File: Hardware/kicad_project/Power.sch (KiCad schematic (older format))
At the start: 23 parts, among them J7 battery, J8 Conn_01x03_Male, Q1 DMG2305UX-13, Q2 Q_PMOS_GSD, Q3 Q_NPN_BEC, SW1 spst_4_pin_internal, U6 MCP73831T-2ATI_OT, U7 AMS1117-3.3

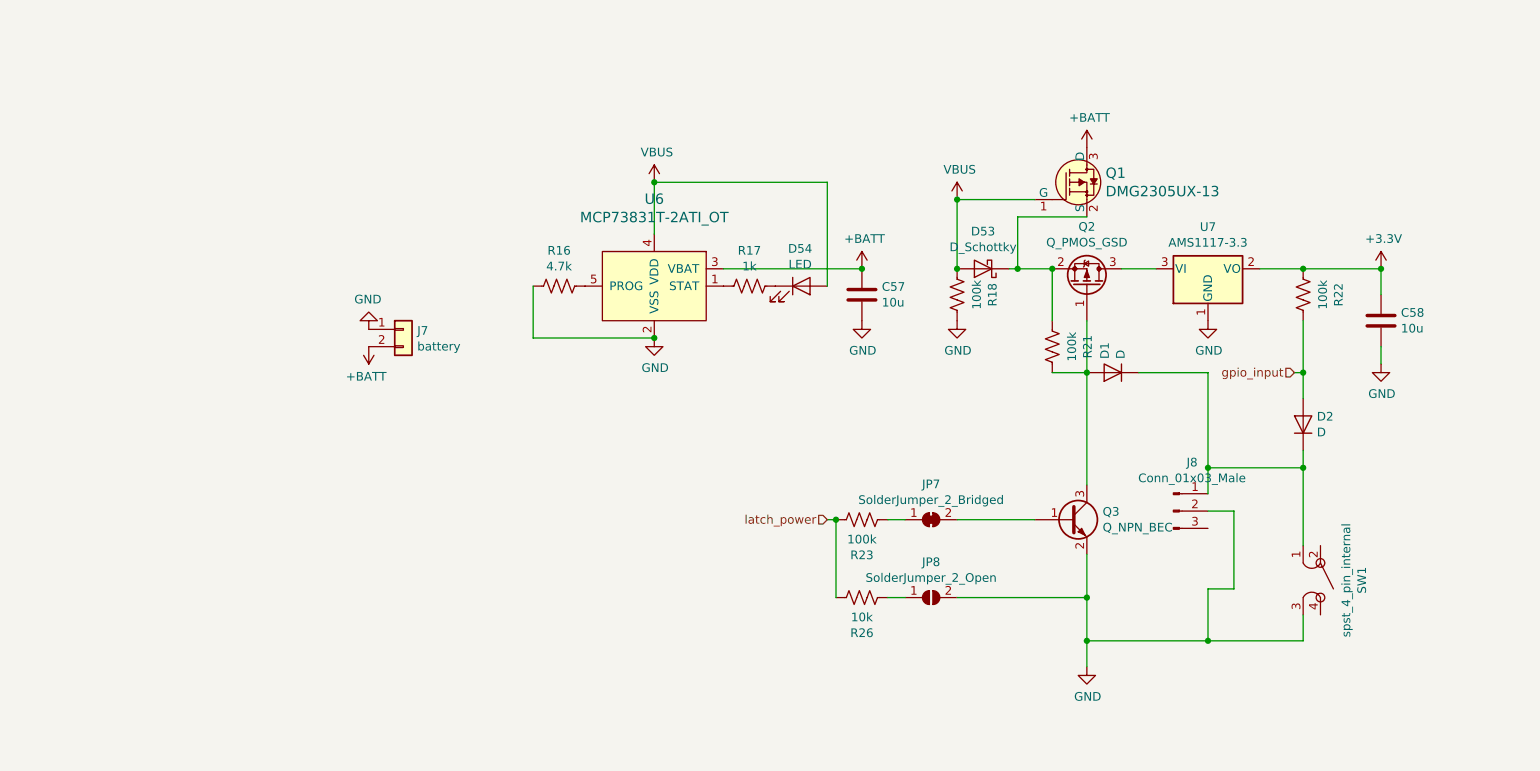
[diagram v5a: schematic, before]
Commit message: new hardware rev
reworked power system
added amp
new LDOS (less dropout)
dedicated LDO for audio system
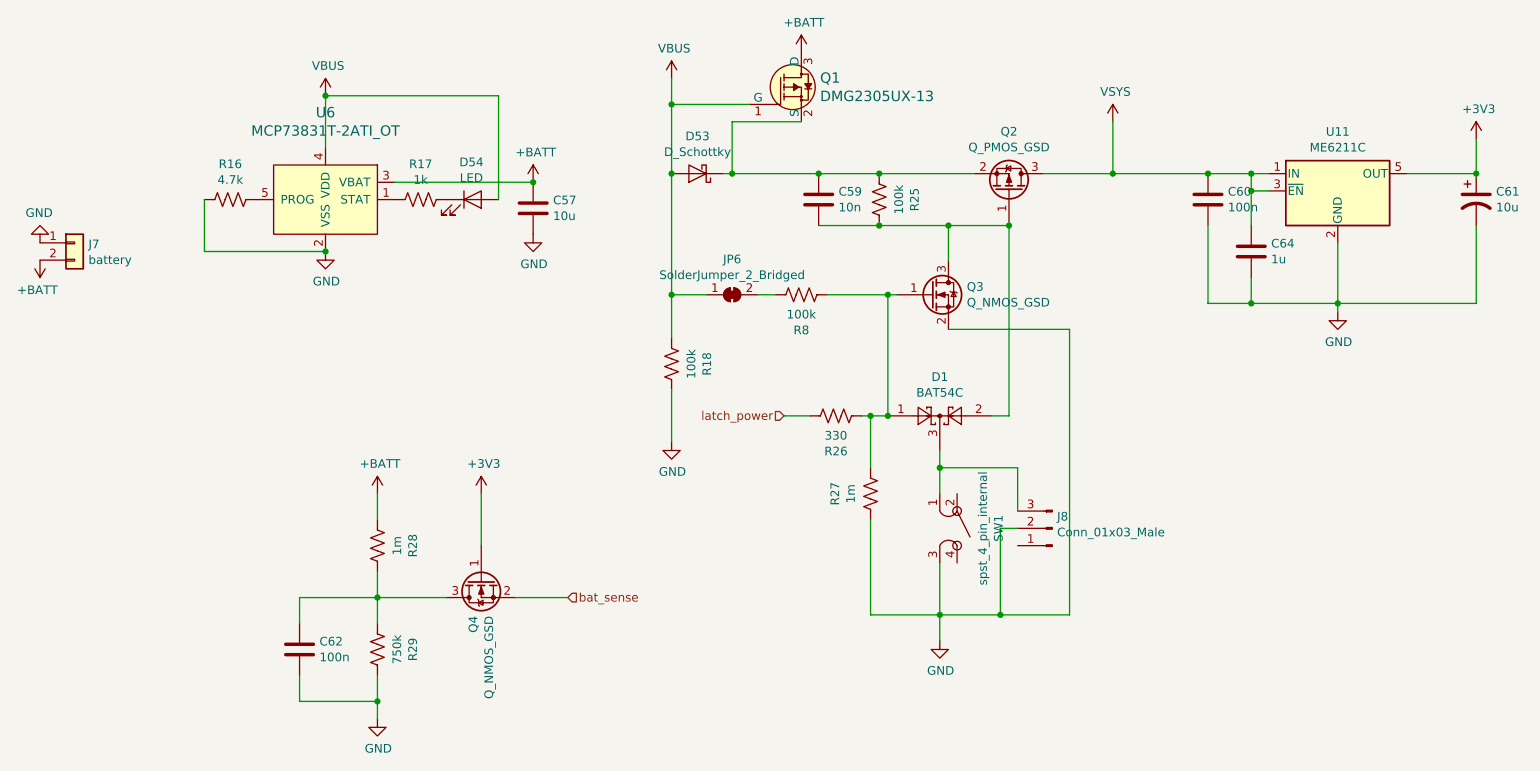
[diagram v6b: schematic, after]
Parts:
- removed C58: 10u, Capacitors_SMD:C_0402_NoSilk, symbol Device:C
- removed D1, D2: D, RandomJunk:D_SOD-323F_less_silk, symbol Device:D
- removed JP7: SolderJumper_2_Bridged, Jumper:SolderJumper-2_P1.3mm_Bridged_RoundedPad1.0x1.5mm, symbol Jumper:SolderJumper_2_Bridged
- removed JP8: SolderJumper_2_Open, Jumper:SolderJumper-2_P1.3mm_Open_RoundedPad1.0x1.5mm, symbol Jumper:SolderJumper_2_Open
- removed Q3: Q_NPN_BEC, TO_SOT_Packages_SMD:SOT-23, symbol Device:Q_NPN_BEC
- removed R21, R22, R23: 100k, Resistors_SMD:R_0402_NoSilk, symbol Device:R_US
- removed U7: AMS1117-3.3, TO_SOT_Packages_SMD:SOT-223, symbol Regulator_Linear:AMS1117-3.3
- added C59: 10n, Capacitors_SMD:C_0402_NoSilk, symbol Device:C
- added C60, C62: 100n, Capacitors_SMD:C_0402_NoSilk, symbol Device:C
- added C61: 10u, Capacitors_SMD:C_0402_NoSilk, symbol Device:CP1
- added C64: 1u, Capacitors_SMD:C_0402_NoSilk, symbol Device:C
- added D1: BAT54C, TO_SOT_Packages_SMD:SOT-23, symbol Diode:BAT54C
- added JP6: SolderJumper_2_Bridged, Jumper:SolderJumper-2_P1.3mm_Bridged_Pad1.0x1.5mm, symbol Jumper:SolderJumper_2_Bridged
- added Q3, Q4: Q_NMOS_GSD, TO_SOT_Packages_SMD:SOT-23, symbol Device:Q_NMOS_GSD
- added R25, R8: 100k, Resistors_SMD:R_0402_NoSilk, symbol Device:R_US
- added R27, R28: 1m, Resistors_SMD:R_0402_NoSilk, symbol Device:R_US
- added R29: 750k, RandomJunk:C_0603_nosilk, symbol Device:R_US
- added U11: ME6211C, TO_SOT_Packages_SMD:SOT-23-5, symbol customLibrary:ME6211C
- J8, U6: checked (none) -> 1
- R18: LCSC C25086 -> C25741
- R26: value 10k -> 330; LCSC C25744 -> C25104
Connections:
- net +3V3: now also C61.1, Q4.1 (G), U11.5 (OUT)
- net +BATT: now also R28.2
- net GND: now also C60.2, C61.2, C62.2, C64.2, Q3.2 (S), R27.2, R29.1, U11.2 (GND)
- net VBUS: now also Q2.3 (D), C60.1, C64.1, JP6.1 (A), U11.1 (IN), U11.3 (~EN~)
- net at Q2.1 (G): now also C59.2, D1.2, Q3.3 (D), R25.1
- net at D53.1 (K), Q1.2 (S), Q2.2 (S): now also C59.1, R25.2
- net at SW1.1: now also J8.3 (Pin_3), D1.3; no longer J8.1 (Pin_1)
- net at R26.2: now also D1.1, Q3.1 (G), R27.1, R8.2
- new net: C62.1, Q4.3 (D), R28.1, R29.2
- new net: JP6.2 (B), R8.1
- new net bat_sense: Q4.2 (S)
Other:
- moved on the sheet: C57, D53, D54, J7, Q1, R16, R17, R18, U6
